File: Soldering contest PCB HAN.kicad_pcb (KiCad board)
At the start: 2 copper layers, 99 x 99 mm, 11 parts, among them J1 Screw_Terminal_01x02, Q1 2N3904, Q2 2N3904

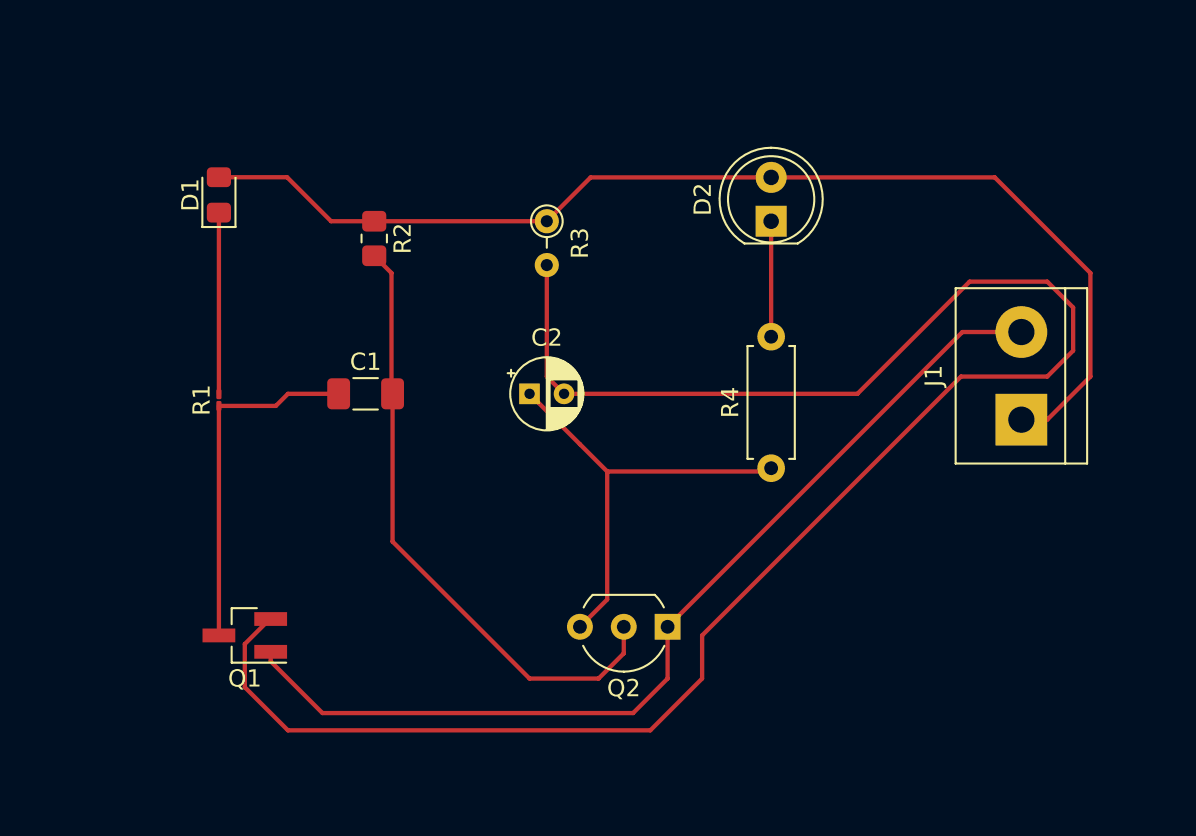
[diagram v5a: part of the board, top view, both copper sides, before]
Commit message: added ground plane
for demonstration purposes
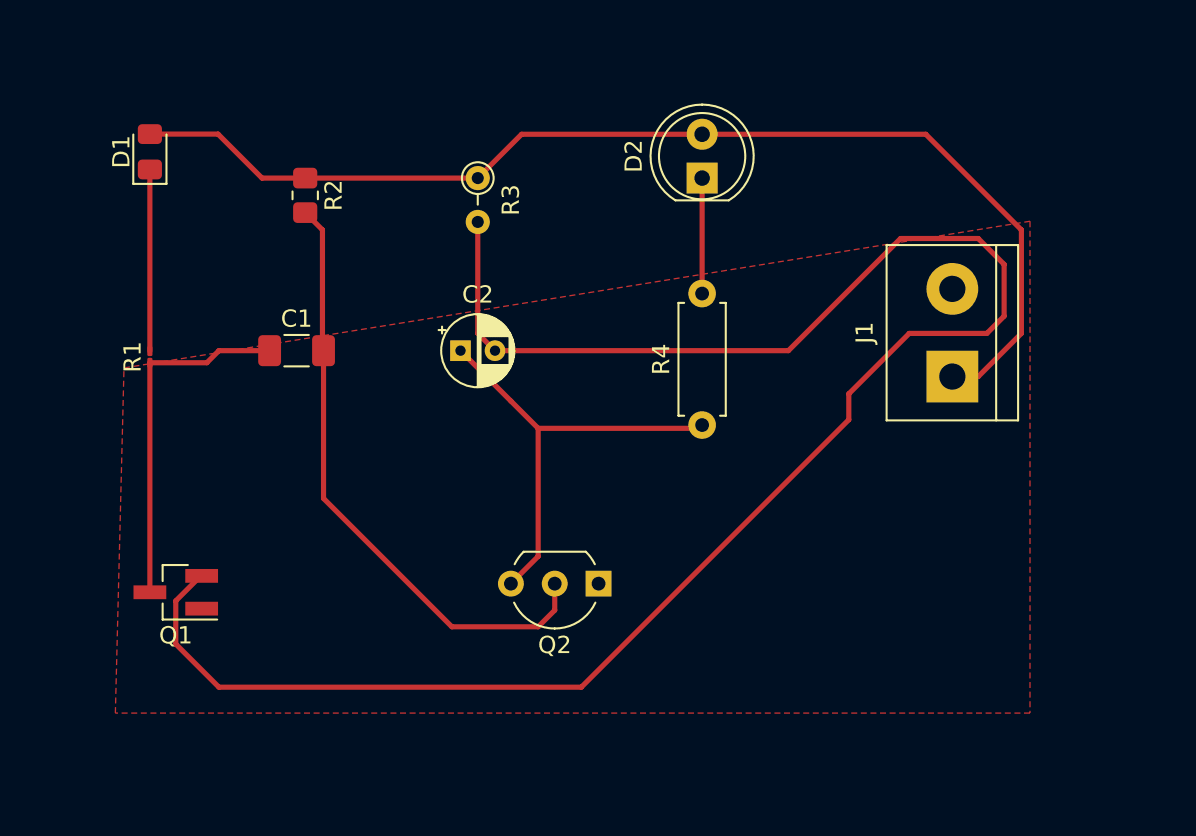
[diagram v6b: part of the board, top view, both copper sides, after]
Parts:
- moved C1 4.72 mm to (145.5, 95.5)
- moved C2 4.72 mm to (155.0, 95.5)
- moved D1 4.72 mm to (137.0, 84.0)
- moved D2 4.72 mm to (169.0, 85.5)
- moved J1 4.72 mm to (183.5, 97.0)
- moved Q1 4.72 mm to (138.5, 109.5)
- moved Q2 4.72 mm to (163.0, 109.0)
- moved R1 4.72 mm to (137.0, 95.9)
- moved R2 4.72 mm to (146.0, 86.5)
- moved R3 4.72 mm to (156.0, 85.5)
- moved R4 4.72 mm to (169.0, 99.8)
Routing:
- net GND: track 56.2 -> 0.00 mm
- added copper zone on F.Cu, net GND

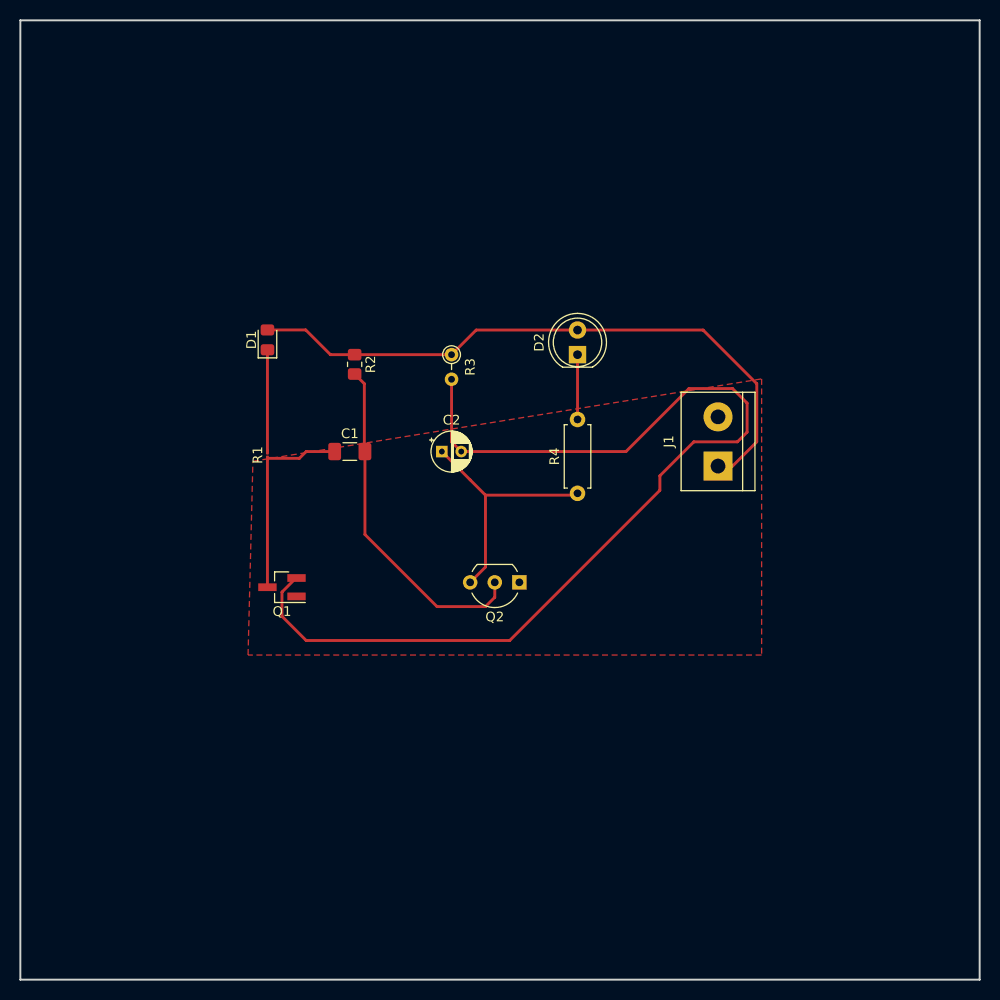
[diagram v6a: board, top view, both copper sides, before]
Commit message: added tips and sponsors to documentation
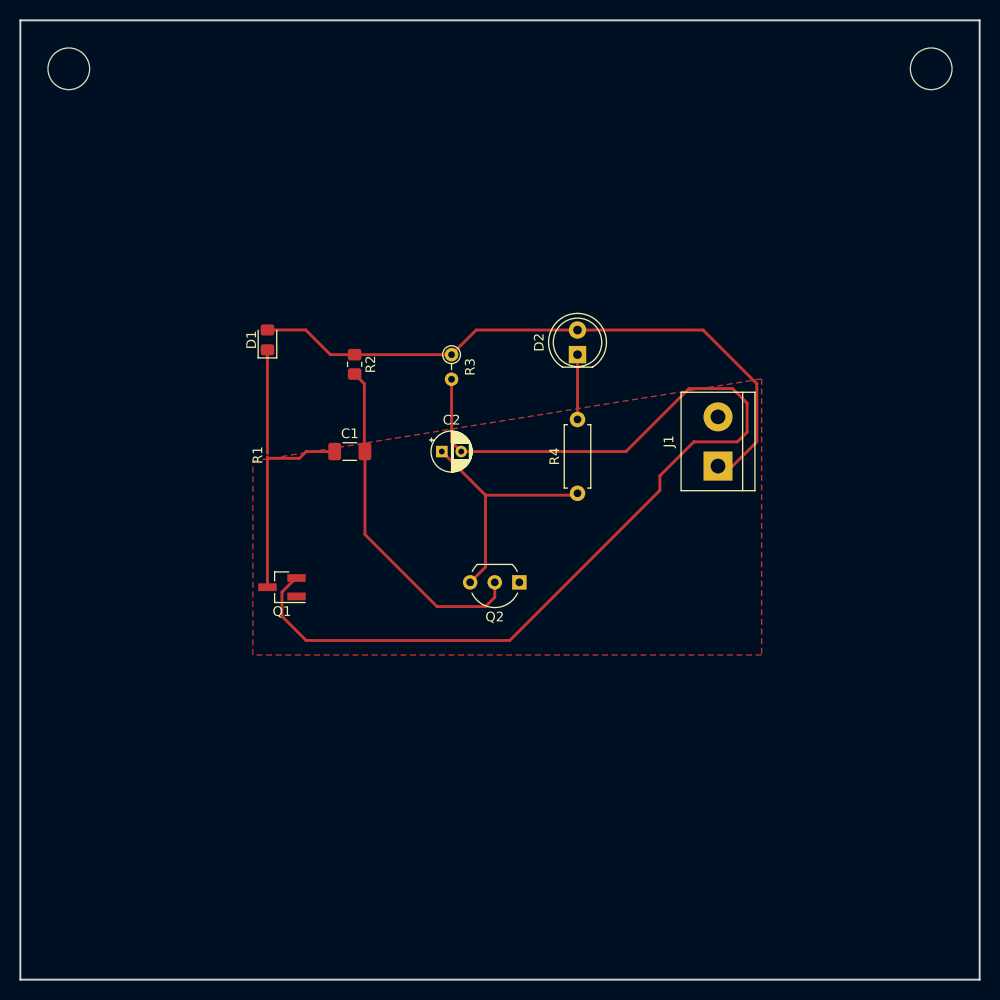
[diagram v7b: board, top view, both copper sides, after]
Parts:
- added REF**: MountingHole_4.3mm_M4, MountingHole:MountingHole_4.3mm_M4, F.Cu at (205.5, 56.0)
- added REF**: MountingHole_4.3mm_M4, MountingHole:MountingHole_4.3mm_M4, F.Cu at (116.5, 56.0)
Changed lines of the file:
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@@
     )
+  )
+  (footprint "MountingHole:MountingHole_4.3mm_M4" (layer "F.Cu")
+    (at 205.5 56)
+    (descr "Mounting Hole 4.3mm, no annular, M4")
+    (tags "mounting hole 4.3mm no annular m4")
+    (attr exclude_from_pos_files exclude_from_bom)
+    (fp_text reference "REF**" (at 0 -5.3) (layer "F.SilkS") hide
+      (effects (font (size 1 1) (thickness 0.15)))
+    )
+    (fp_text value "MountingHole_4.3mm_M4" (at 0 5.3) (layer "F.Fab")
+      (effects (font (size 1 1) (thickness 0.15)))
+    )
+    (fp_text user "${REFERENCE}" (at 0 0) (layer "F.Fab")
+      (effects (font (size 1 1) (thickness 0.15)))
+    )
+    (fp_circle (center 0 0) (end 4.3 0) (layer "Cmts.User") (width 0.15) (fill none))
+    (fp_circle (center 0 0) (end 4.55 0) (layer "F.CrtYd") (width 0.05) (fill none))
+    (pad "" np_thru_hole circle (at 0 0) (size 4.3 4.3) (drill 4.3) (layers *.Cu *.Mask))
   )
   (footprint "LED_THT:LED_D5.0mm_Clear" (layer "F.Cu")
@@
     )
   )
+  (footprint "MountingHole:MountingHole_4.3mm_M4" (layer "F.Cu")
+    (at 116.5 56)
+    (descr "Mounting Hole 4.3mm, no annular, M4")
+    (tags "mounting hole 4.3mm no annular m4")
+    (attr exclude_from_pos_files exclude_from_bom)
+    (fp_text reference "REF**" (at 0 -5.3) (layer "F.SilkS") hide
+      (effects (font (size 1 1) (thickness 0.15)))
+    )
+    (fp_text value "MountingHole_4.3mm_M4" (at 0 5.3) (layer "F.Fab")
+      (effects (font (size 1 1) (thickness 0.15)))
+    )
+    (fp_text user "${REFERENCE}" (at 0 0) (layer "F.Fab")
+      (effects (font (size 1 1) (thickness 0.15)))
+    )
+    (fp_circle (center 0 0) (end 4.3 0) (layer "Cmts.User") (width 0.15) (fill none))
+    (fp_circle (center 0 0) (end 4.55 0) (layer "F.CrtYd") (width 0.05) (fill none))
+    (pad "" np_thru_hole circle (at 0 0) (size 4.3 4.3) (drill 4.3) (layers *.Cu *.Mask))
+  )
   (footprint "Package_TO_SOT_THT:TO-92_Inline_Wide" (layer "F.Cu")
     (at 163 109 180)
@@
       (pts
         (xy 188 116.5)
-        (xy 135 116.5)
+        (xy 135.5 116.5)
         (xy 135.5 96.5)
         (xy 188 88)

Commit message: started on silkscreen
added student and grade boxes
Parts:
- moved C1 1.84 mm to (147.3, 95.5)
- moved C2 1.84 mm to (156.8, 95.5)
- moved D1 1.84 mm to (138.8, 84.0)
- moved D2 1.84 mm to (170.8, 85.5)
- moved J1 1.84 mm to (185.3, 97.0)
- moved Q1 1.84 mm to (140.3, 109.5)
- moved Q2 1.84 mm to (164.8, 109.0)
- moved R1 1.84 mm to (138.8, 95.9)
- moved R2 1.84 mm to (147.8, 86.5)
- moved R3 1.84 mm to (157.8, 85.5)
- moved R4 1.84 mm to (170.8, 99.8)
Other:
- board text added: "GRADE"
- board text added: "STUDENT"
